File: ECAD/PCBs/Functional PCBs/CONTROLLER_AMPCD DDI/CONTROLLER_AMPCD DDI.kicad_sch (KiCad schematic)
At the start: 28 parts, among them J1 BUS IN, J2 BUS OUT, J3 DDI/AMPCD, J4 BRT/CRS, J5 CONT/HDG, J6 DDI ROT, J7 AMPCD ROT, J8 EWI SW, Q1 IRFB3206PBF, Q2 IRLML6402TRPBF, U1 MAX487EESA+T

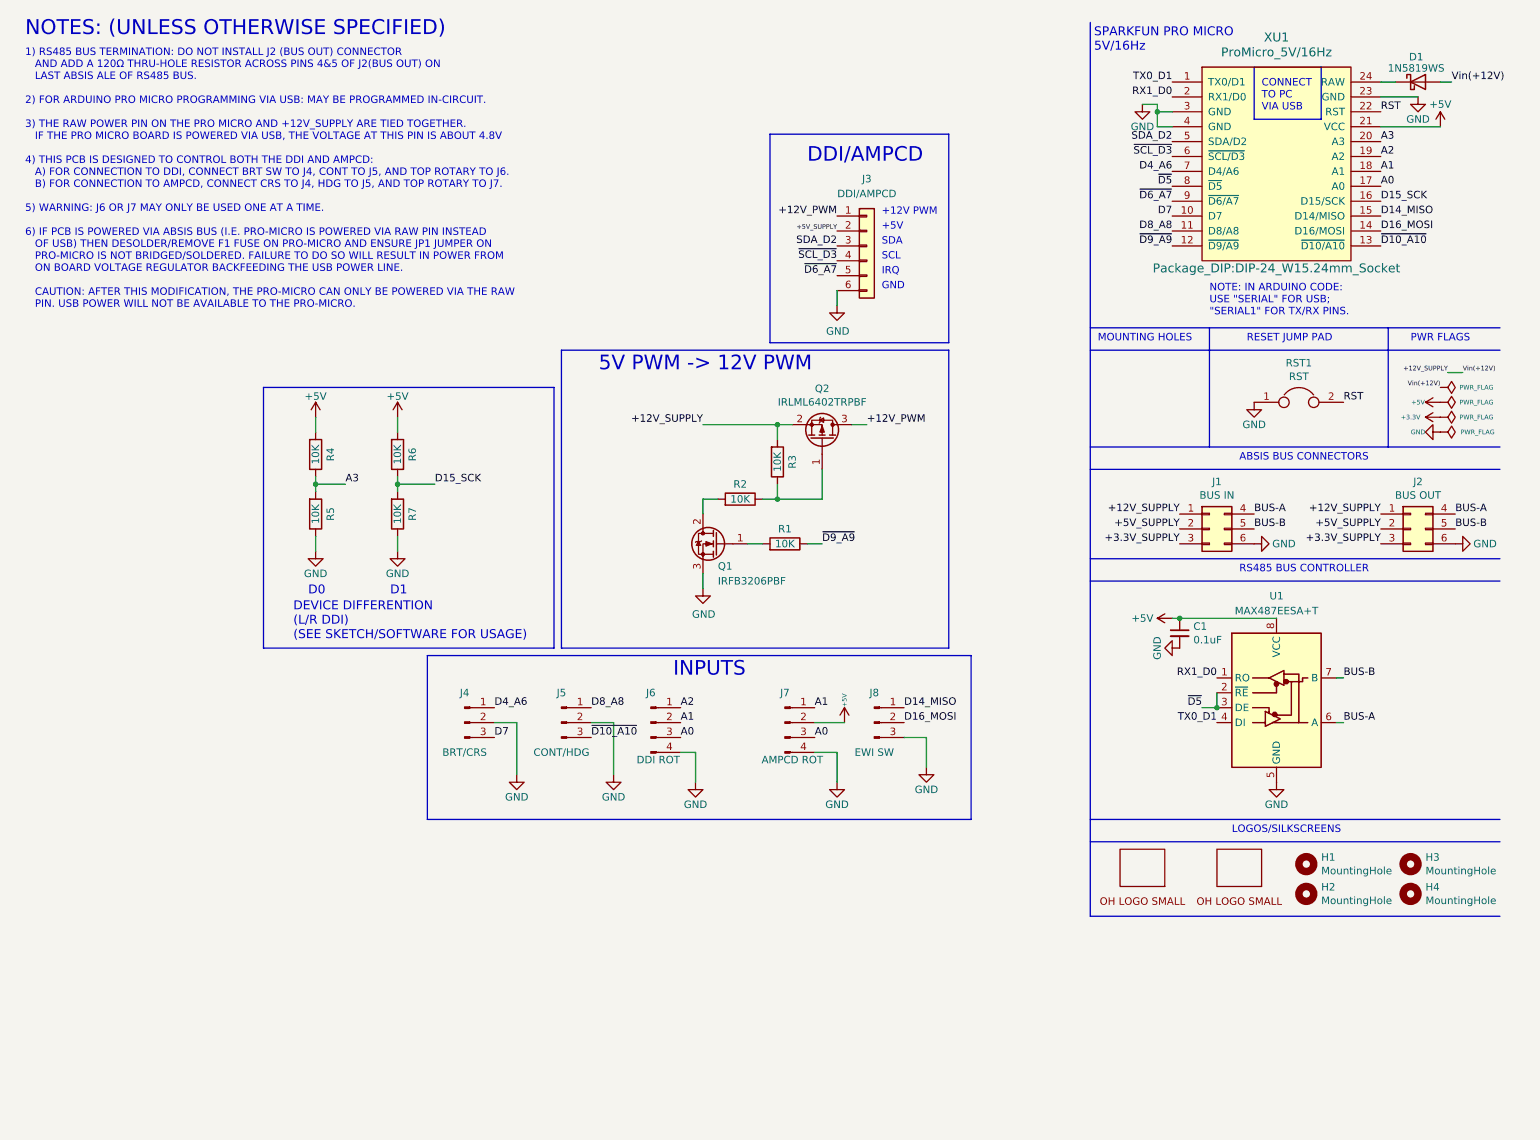
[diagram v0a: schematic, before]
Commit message: RS-485 Update across ABSIS and New Power
RS-485 Update across ABSIS and New Power
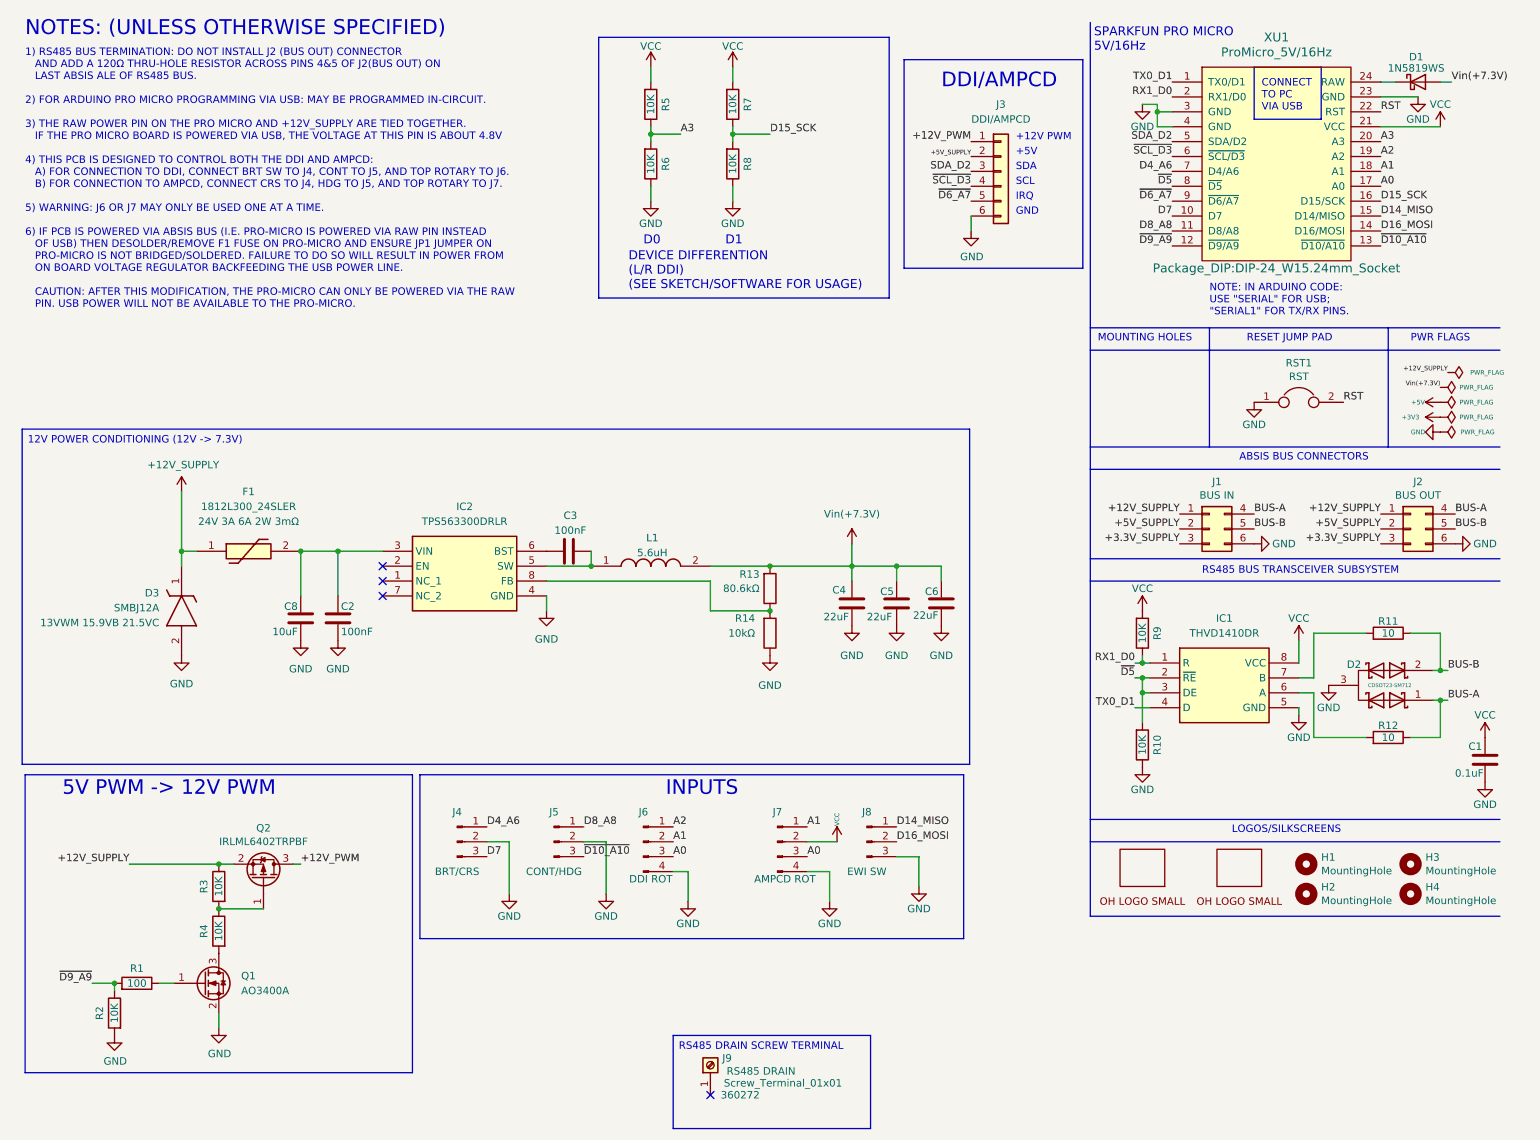
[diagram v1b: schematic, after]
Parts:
- removed C1: 0.1uF, Capacitor_SMD:C_0805_2012Metric, symbol Device:C_Small
- removed Q1: IRFB3206PBF, Package_TO_SOT_THT:TO-220-3_Vertical, symbol Device:Q_NMOS_GDS
- removed U1: MAX487EESA+T, Package_SO:SOIC-8_3.9x4.9mm_P1.27mm, symbol Interface_UART:MAX487E
- added C1: 0.1uF, OH_Footprints:C_0603_1608Metric, symbol OH_Symbols:Capacitor_0603_0.1uF
- added C2, C3: 100nF, Capacitor_SMD:C_0402_1005Metric, symbol Device:C
- added C4, C5, C6: 22uF, Capacitor_SMD:C_0805_2012Metric, symbol Device:C
- added C8: 10uF, Capacitor_SMD:C_0603_1608Metric, symbol Device:C
- added D2: CDSOT23-SM712, OH_Footprints:CDSOT23-SM712, symbol OH_Symbols:CDSOT23-SM712
- added D3: SMBJ12A, Diode_SMD:D_SMB, symbol SMBJ12A:SMBJ12A
- added F1: 1812L300_24SLER, Fuse:Fuse_1812_4532Metric, symbol 1812L300_24SLER:1812L300_24SLER
- added IC1: THVD1410DR, OH_Footprints:THVD1410DR, symbol OH_Symbols:THVD1410DR
- added IC2: TPS563300DRLR, Package_TO_SOT_SMD:SOT-583-8, symbol TPS563300DRLR:TPS563300DRLR
- added J9: Screw_Terminal_01x01, TerminalBlock_MetzConnect:TerminalBlock_MetzConnect_360272_1x01_Horizontal_ScrewM2.6, symbol Connector:Screw_Terminal_01x01
- added L1: 5.6uH, Inductor_SMD:L_Bourns_SRP6060FA, symbol SRP6060FA-5R6M:SRP6060FA-5R6M
- added Q1: AO3400A, Package_TO_SOT_SMD:SOT-23, symbol Transistor_FET:AO3400A
- added R10, R4, R9: 10K, Resistor_SMD:R_0603_1608Metric_Pad0.98x0.95mm_HandSolder, symbol Device:R
- added R11, R12: 10, Resistor_SMD:R_0603_1608Metric_Pad0.98x0.95mm_HandSolder, symbol OH_Symbols:Resistor_0603_10Ω
- added R13: 80.6kΩ, Resistor_SMD:R_0402_1005Metric, symbol Device:R
- added R14: 10kΩ, Resistor_SMD:R_0402_1005Metric, symbol Device:R
- LOGO1: footprint KiCAD Libraries:OH_LOGO_ONLY_11x6mm -> OH_Footprints:LOGO_OH_NoText_Small
- LOGO2: footprint KiCAD Libraries:OH_LOGO_ONLY_11x6mm -> OH_Footprints:LOGO_OH_Text_Small
- R1: value 10K -> 100
- renumbered R4 to R5, R5 to R6, R6 to R7, R7 to R8
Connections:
- net +12V_SUPPLY: now also R3.1, D3.1 (K), F1.1; no longer D1.2 (A), R3.2
- net +5V: no longer J7.2 (Pin_2), R5.2, R7.2, XU1.21 (VCC)
- net BUS-A: now also D2.1, R12.2
- net BUS-B: now also D2.2, R11.2
- net GND: now also R2.2, C1.1, C2.1, C4.2, C5.2, C6.2, C8.1, D2.3, D3.2 (A), IC1.5 (GND), IC2.4 (GND), Q1.2 (S), R10.1, R14.1
- net RX1_D0: now also IC1.1 (R), R9.1
- net TX0_D1: now also IC1.4 (D)
- net ~{D5}: now also IC1.2 (~{RE}), IC1.3 (DE), R10.2
- net ~{D9_A9}: now also R1.2, R2.1; no longer R1.1
- new net: Q1.1 (G), R1.1
- new net: Q2.1 (G), R3.2, R4.1
- new net: Q1.3 (D), R4.2
- new net: IC1.6 (A), R12.1
- new net: IC1.7 (B), R11.1
- new net: C2.2, C8.2, F1.2, IC2.3 (VIN)
- new net: IC2.8 (FB), R13.1, R14.2
- new net: C3.1, IC2.5 (SW), L1.1
- new net: C3.2, IC2.6 (BST)
- new net VCC: C1.2, IC1.8 (VCC), J7.2 (Pin_2), R5.2, R7.2, R9.2, XU1.21 (VCC)
- new net Vin(+7.3V): C4.1, C5.1, C6.1, D1.2 (A), L1.2, R13.2
- no-connect marks 0 -> 4
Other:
- note added: "RS485 BUS TRANSCEIVER SUBSYSTEM"
- note removed: "RS485 BUS CONTROLLER"
- moved on the sheet: J3, J4, J5, J6, J7, J8, Q2, R1, R3, R5, R6, R7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

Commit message: Continue work on RS485 and Power board Layout
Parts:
- removed C6: 22uF, Capacitor_SMD:C_0805_2012Metric, symbol Device:C
- removed J9: Screw_Terminal_01x01, TerminalBlock_MetzConnect:TerminalBlock_MetzConnect_360272_1x01_Horizontal_ScrewM2.6, symbol Connector:Screw_Terminal_01x01
- added R13: 0, Resistor_SMD:R_0402_1005Metric, symbol Device:R
- D3: symbol SMBJ12A:SMBJ12A -> OH_Symbols:SMBJ12A
- F1: symbol 1812L300_24SLER:1812L300_24SLER -> OH_Symbols:1812L300_24SLER
- IC2: symbol TPS563300DRLR:TPS563300DRLR -> OH_Symbols:TPS563300DRLR; Height (none) -> 0.6; Manufacturer_Part_Number (none) -> 595-TPS563300; Mouser Part Number (none) -> 595-TPS563300DRLR
- L1: symbol SRP6060FA-5R6M:SRP6060FA-5R6M -> OH_Symbols:SRP6060FA-5R6M
- Q1: symbol Transistor_FET:AO3400A -> OH_Symbols:AO3400A
- Q2: symbol Transistor_FET:IRLML6402 -> OH_Symbols:IRLML6402
- renumbered C8 to C2, C2 to C3, C3 to C4, C4 to C5, C5 to C6, R13 to R14, R14 to R15
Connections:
- net at IC2.6 (BST): now also R13.1; no longer C4.2
- net BUS-A renamed BUS_P
- net BUS-B renamed BUS_N
- new net: C4.2, R13.2
- no-connect marks 4 -> 3
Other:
- moved on the sheet: C4, C5, C6, L1, R14, R15

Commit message: Added Notes and Fiducials
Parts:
- added FID1, FID2, FID3: Fiducial, Fiducial:Fiducial_1mm_Mask2mm, symbol OH_Symbols:Fiducial
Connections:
- net BUS_N renamed BUS-B
- net BUS_P renamed BUS-A
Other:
- note added: "1) RS485 BUS TERMINATION: DO NOT INSTALL J2 (BUS OUT) CONNECTOR AND ADD A 120Ω THRU-HOLE RESISTOR ACROSS PINS 4&5 OF J2(BUS OUT) ON LAST ABSIS ALE OF RS485 BUS. 2) FOR ARDUINO PRO MICRO PROGRAMMING VIA USB: MAY BE PROGRAMMED IN-CIRCUIT. 3) THE RAW POWER PIN ON THE PRO MICRO AND Vin(+7.3V) ARE TIED TOGETHER. IF THE PRO MICRO BOARD IS POWERED VIA USB, THE VOLTAGE AT THIS PIN IS ABOUT 4.8V (needs to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"
- note added: "FIDUCIALS"
- note removed: "1) RS485 BUS TERMINATION: DO NOT INSTALL J2 (BUS OUT) CONNECTOR AND ADD A 120Ω THRU-HOLE RESISTOR ACROSS PINS 4&5 OF J2(BUS OUT) ON LAST ABSIS ALE OF RS485 BUS. 2) FOR ARDUINO PRO MICRO PROGRAMMING VIA USB: MAY BE PROGRAMMED IN-CIRCUIT. 3) THE RAW POWER PIN ON THE PRO MICRO AND +12V_SUPPLY ARE TIED TOGETHER. IF THE PRO MICRO BOARD IS POWERED VIA USB, THE VOLTAGE AT THIS PIN IS ABOUT 4.8V 4) THIS 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"
- note removed: "MOUNTING HOLES"

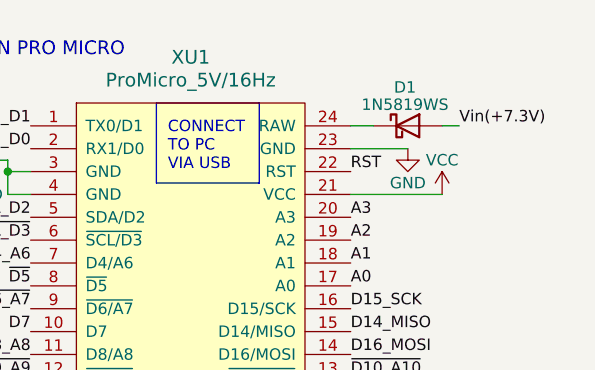
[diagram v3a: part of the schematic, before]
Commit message: Migrate symbols from old libraries to OH_symbol
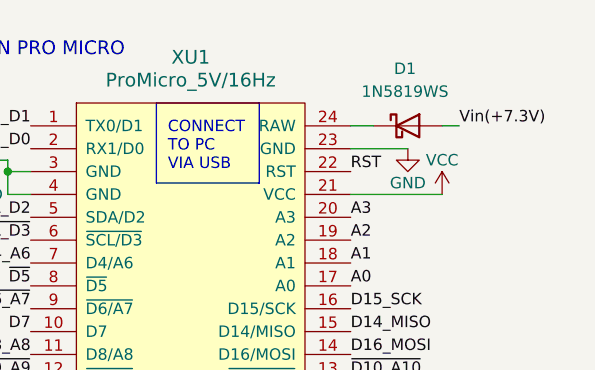
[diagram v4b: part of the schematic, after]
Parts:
- D1: symbol Device:D_Schottky -> OH_Symbols:1N5819WS
- J1, J2: symbol Connector_Generic:Conn_02x03_Top_Bottom -> OH_Symbols:Conn_02x03_Top_Bottom
- J3: symbol Connector_Generic:Conn_01x06 -> OH_Symbols:Conn_01x06
- J4, J5, J8: symbol Connector:Conn_01x03_Male -> OH_Symbols:Conn_01x03_Male
- J6, J7: symbol Connector:Conn_01x04_Male -> OH_Symbols:Conn_01x04_Male
- RST1: symbol CONTROLLER,-AMPCD_DDI-rescue:Jumper-Device -> OH_Symbols:Jumper-Device
- XU1: symbol KiCadCustomLib:ProMicro -> OH_Symbols:ProMicro
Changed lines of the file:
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@@
 	)
 	(symbol
-		(lib_id "Connector:Conn_01x03_Male")
+		(lib_id "OH_Symbols:Conn_01x03_Male")
 		(at 87.63 153.67 0)
 		(unit 1)
@@
 	)
 	(symbol
-		(lib_id "Connector:Conn_01x03_Male")
+		(lib_id "OH_Symbols:Conn_01x03_Male")
 		(at 104.14 153.67 0)
 		(unit 1)
@@
 	)
 	(symbol
-		(lib_id "Connector:Conn_01x04_Male")
+		(lib_id "OH_Symbols:Conn_01x04_Male")
 		(at 119.38 153.67 0)
 		(unit 1)
@@
 	)
 	(symbol
-		(lib_id "Connector_Generic:Conn_02x03_Top_Bottom")
+		(lib_id "OH_Symbols:Conn_02x03_Top_Bottom")
 		(at 215.9 100.33 0)
 		(unit 1)
@@
 			)
 		)
-		(property "Description" ""
+		(property "Description" "Generic connector, double row, 02x03, top/bottom pin numbering scheme (row 1: 1...pins_per_row, row2: pins_per_row+1 ... num_pins), script generated (kicad-library-utils/schlib/autogen/connector/)"
 			(at 215.9 100.33 0)
+			(hide yes)
 			(show_name no)
 			(do_not_autoplace no)
@@
 	)
 	(symbol
-		(lib_id "Connector_Generic:Conn_02x03_Top_Bottom")
+		(lib_id "OH_Symbols:Conn_02x03_Top_Bottom")
 		(at 250.19 100.33 0)
 		(unit 1)
@@
 			)
 		)
-		(property "Description" ""
+		(property "Description" "Generic connector, double row, 02x03, top/bottom pin numbering scheme (row 1: 1...pins_per_row, row2: pins_per_row+1 ... num_pins), script generated (kicad-library-utils/schlib/autogen/connector/)"
 			(at 250.19 100.33 0)
+			(hide yes)
 			(show_name no)
 			(do_not_autoplace no)
@@
 	)
 	(symbol
-		(lib_id "Connector_Generic:Conn_01x06")
+		(lib_id "OH_Symbols:Conn_01x06")
 		(at 180.34 39.37 0)
 		(unit 1)
@@
 	)
 	(symbol
-		(lib_id "Connector:Conn_01x03_Male")
+		(lib_id "OH_Symbols:Conn_01x03_Male")
 		(at 157.48 153.67 0)
 		(unit 1)
@@
 	)
 	(symbol
-		(lib_id "Connector:Conn_01x04_Male")
+		(lib_id "OH_Symbols:Conn_01x04_Male")
 		(at 142.24 153.67 0)
 		(unit 1)
@@
 	)
 	(symbol
-		(lib_id "KiCadCustomLib:ProMicro")
+		(lib_id "OH_Symbols:ProMicro")
 		(at 227.33 43.18 0)
 		(unit 1)
@@
 	)
 	(symbol
-		(lib_id "CONTROLLER,-AMPCD_DDI-rescue:Jumper-Device")
+		(lib_id "OH_Symbols:Jumper-Device")
 		(at 231.14 78.74 0)
 		(unit 1)
@@
 	)
 	(symbol
-		(lib_id "Device:D_Schottky")
+		(lib_id "OH_Symbols:1N5819WS")
 		(at 251.46 24.13 0)
 		(unit 1)
@@
 		(fields_autoplaced yes)
 		(property "Reference" "D1"
-			(at 251.1425 19.8501 0)
+			(at 251.1425 17.78 0)
 			(show_name no)
 			(do_not_autoplace no)
@@
 		)
 		(property "Value" "1N5819WS"
-			(at 251.1425 21.7711 0)
+			(at 251.1425 20.32 0)
 			(show_name no)
 			(do_not_autoplace no)

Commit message: Updating Symbols to new/corrected library entries
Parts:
- C2: symbol Device:C -> OH_Symbols:Capacitor_0603_10uF
- C3: symbol Device:C -> OH_Symbols:Capacitor_0402_0.1uF
- D2: LCSC (none) -> C404012
- IC1: LCSC (none) -> C2671345
- Q1: LCSC (none) -> C20917; Manufacture PN (none) -> AO3400A
- R1: symbol Device:R -> OH_Symbols:Resistor_0603_100Ω; LCSC C25804 -> C22775; PN 0603WAF1002T5E -> 0603WAF1000T5E
- R13: symbol Device:R -> OH_Symbols:Resistor_0402_0Ω; LCSC (none) -> C17168; Manufacture PN (none) -> 0402WGF0000TCE
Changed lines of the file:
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@@
 	)
 	(symbol
-		(lib_id "Device:R")
+		(lib_id "OH_Symbols:Resistor_0603_100Ω")
 		(at 33.02 177.8 270)
 		(mirror x)
@@
 			)
 		)
-		(property "Datasheet" "https://datasheet.lcsc.com/szlcsc/1811062009_UNI-ROYAL-Uniroyal-Elec-0603WAF1002T5E_C25804.pdf"
+		(property "Datasheet" "https://www.lcsc.com/datasheet/C22775.pdf"
 			(at 33.02 177.8 0)
 			(hide yes)
@@
 			)
 		)
-		(property "Description" ""
+		(property "Description" "Resistor,, SMD 0603_1608, 100 Ohm"
 			(at 33.02 177.8 0)
+			(hide yes)
 			(show_name no)
 			(do_not_autoplace no)
@@
 			)
 		)
-		(property "PN" "0603WAF1002T5E"
+		(property "PN" "0603WAF1000T5E"
 			(at 33.02 177.8 90)
 			(hide yes)
@@
 			)
 		)
-		(property "LCSC" "C25804"
+		(property "LCSC" "C22775"
 			(at 33.02 177.8 90)
 			(hide yes)
@@
 			)
 		)
+		(property "LCSC" "C20917"
+			(at 44.45 177.8 0)
+			(hide yes)
+			(show_name no)
+			(do_not_autoplace no)
+			(effects
+				(font
+					(size 1.27 1.27)
+				)
+			)
+		)
+		(property "Manufacture PN" "AO3400A"
+			(at 44.45 177.8 0)
+			(hide yes)
+			(show_name no)
+			(do_not_autoplace no)
+			(effects
+				(font
+					(size 1.27 1.27)
+				)
+			)
+		)
 		(pin "1"
 		)
@@
 			)
 		)
+		(property "LCSC" "C2671345"
+			(at 205.74 123.19 0)
+			(hide yes)
+			(show_name no)
+			(do_not_autoplace no)
+			(effects
+				(font
+					(size 1.27 1.27)
+				)
+			)
+		)
 		(pin "8"
 		)
@@
 	)
 	(symbol
-		(lib_id "Device:C")
+		(lib_id "OH_Symbols:Capacitor_0402_0.1uF")
 		(at 67.31 115.57 180)
 		(unit 1)
@@
 			)
 		)
-		(property "Description" ""
+		(property "Description" "Capacitor, Non-polarized, SMD 0402_1005, 0.1uF"
 			(at 70.231 117.9943 0)
+			(hide yes)
 			(show_name no)
 			(do_not_autoplace no)
@@
 	)
 	(symbol
-		(lib_id "Device:R")
+		(lib_id "OH_Symbols:Resistor_0402_0Ω")
 		(at 106.68 104.14 90)
 		(unit 1)
@@
 			)
 		)
-		(property "Datasheet" ""
+		(property "Datasheet" "https://www.lcsc.com/datasheet/C17168.pdf"
+			(at 106.68 104.14 0)
+			(hide yes)
+			(show_name no)
+			(do_not_autoplace no)
+			(effects
+				(font
+					(size 1.27 1.27)
+				)
+			)
+		)
+		(property "Description" "Resistor,, SMD 0402_1005, 0 Ohm"
+			(at 106.68 104.14 0)
+			(hide yes)
+			(show_name no)
+			(do_not_autoplace no)
+			(effects
+				(font
+					(size 1.27 1.27)
+				)
+			)
+		)
+		(property "LCSC" "C17168"
 			(at 106.68 104.14 0)
 			(hide yes)
@@
 			)
 		)
-		(property "Description" "Resistor"
+		(property "Manufacture PN" "0402WGF0000TCE"
 			(at 106.68 104.14 0)
 			(hide yes)
@@
 	)
 	(symbol
-		(lib_id "Device:C")
+		(lib_id "OH_Symbols:Capacitor_0603_10uF")
 		(at 60.96 115.57 0)
 		(mirror x)
@@
 			)
 		)
-		(property "Description" ""
+		(property "Description" "Capacitor, Non-polarized, SMD 0603_1608, 10uF"
 			(at 58.039 117.9943 0)
+			(hide yes)
 			(show_name no)
 			(do_not_autoplace no)
@@
 			)
 		)
+		(property "LCSC" "C404012"
+			(at 246.38 127 0)
+			(hide yes)
+			(show_name no)
+			(do_not_autoplace no)
+			(effects
+				(font
+					(size 1.27 1.27)
+				)
+			)
+		)
